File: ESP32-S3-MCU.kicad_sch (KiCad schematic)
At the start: 40 parts, among them SW1 RESET, SW2 BOOT, X1 32.768KHz

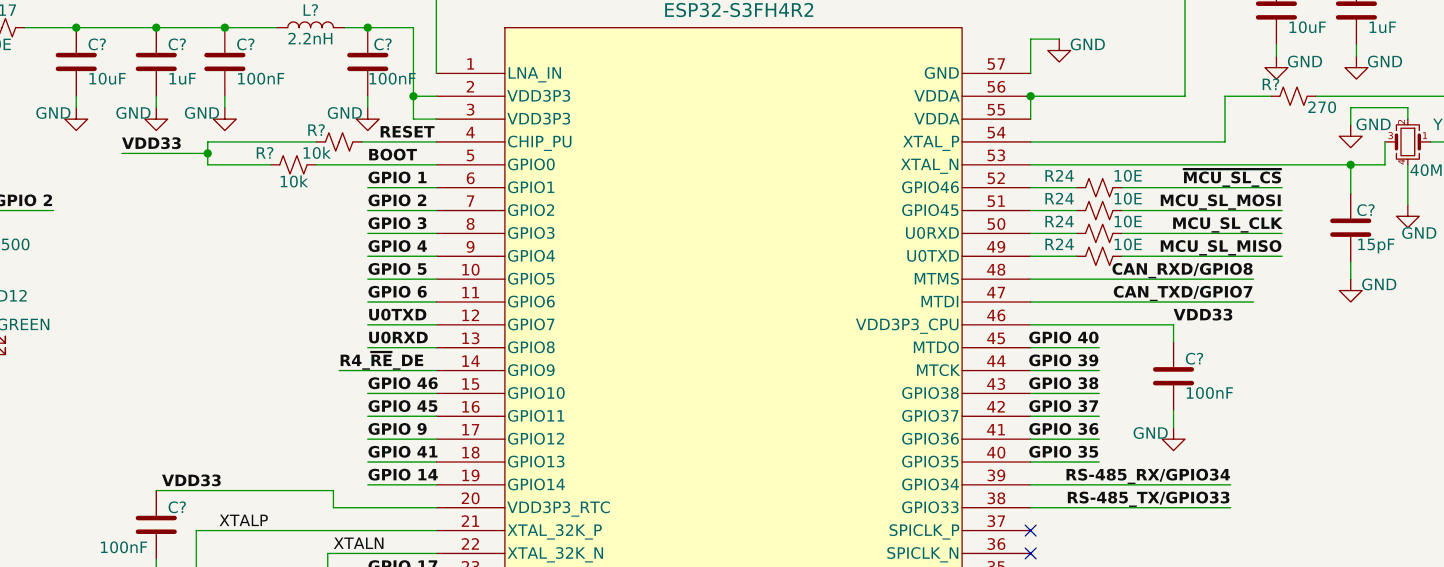
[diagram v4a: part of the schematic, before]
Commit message: Changed UART0 port connections
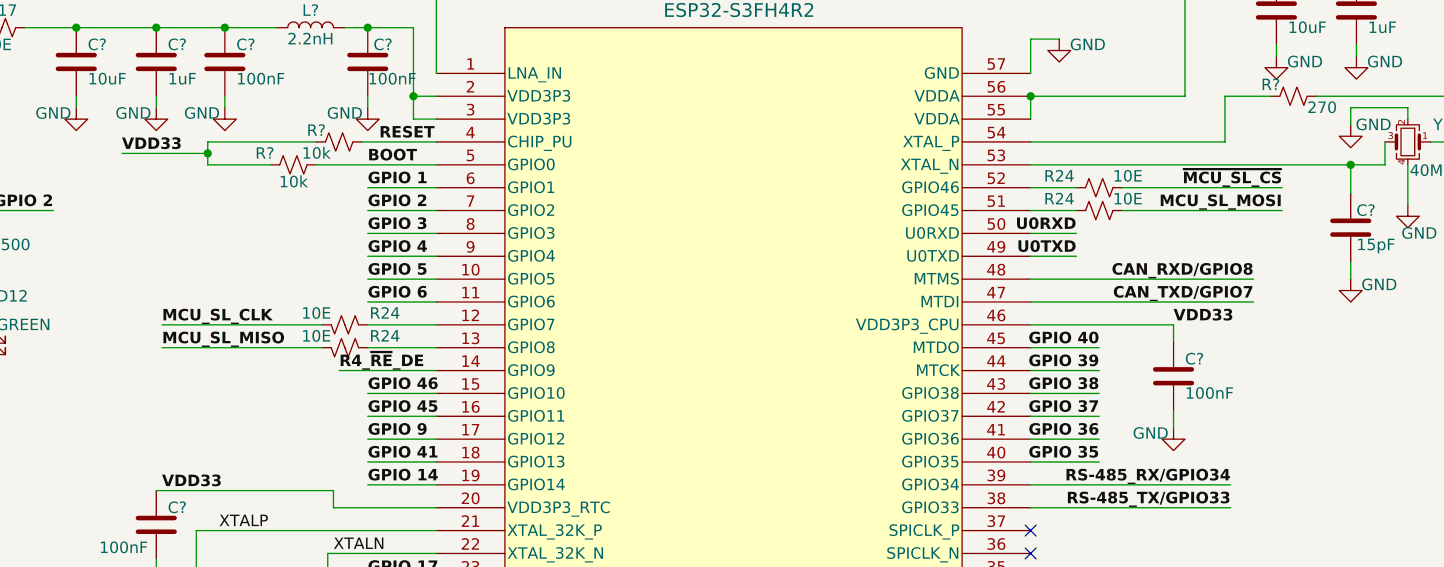
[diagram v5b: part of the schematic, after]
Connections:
- net BOOT_RXD: now also U?.50 (U0RXD); no longer U?.13 (GPIO8)
- net BOOT_TXD: now also U?.49 (U0TXD); no longer U?.12 (GPIO7)
- net at R24.1: now also U?.12 (GPIO7); no longer U?.50 (U0RXD)
- net at R24.2: now also U?.13 (GPIO8); no longer U?.49 (U0TXD)
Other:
- moved on the sheet: R24
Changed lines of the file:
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@@
     (stroke (width 0) (type default))
   )
-  (wire (pts (xy 215.265 80.01) (xy 197.485 80.01))
+  (wire (pts (xy 90.805 90.17) (xy 108.585 90.17))
     (stroke (width 0) (type default))
   )
@@
     (stroke (width 0) (type default))
   )
-  (wire (pts (xy 215.265 82.55) (xy 197.485 82.55))
+  (wire (pts (xy 90.805 92.71) (xy 108.585 92.71))
     (stroke (width 0) (type default))
   )
@@
     (effects (font (size 1.27 1.27) (thickness 0.254) bold (color 204 102 0 1)) (justify right bottom))
   )
-  (label "U0RXD" (at 113.665 92.71 0) (fields_autoplaced)
-    (effects (font (size 1.27 1.27) bold (color 0 0 255 1)) (justify left bottom))
-  )
-  (label "MCU_SL_MISO" (at 215.265 82.55 180) (fields_autoplaced)
-    (effects (font (size 1.27 1.27) (thickness 0.254) bold (color 204 102 0 1)) (justify right bottom))
-  )
-  (label "MCU_SL_CLK" (at 215.265 80.01 180) (fields_autoplaced)
-    (effects (font (size 1.27 1.27) (thickness 0.254) bold (color 204 102 0 1)) (justify right bottom))
+  (label "U0RXD" (at 192.405 80.01 180) (fields_autoplaced)
+    (effects (font (size 1.27 1.27) bold (color 0 0 255 1)) (justify right bottom))
+  )
+  (label "MCU_SL_MISO" (at 90.805 92.71 0) (fields_autoplaced)
+    (effects (font (size 1.27 1.27) (thickness 0.254) bold (color 204 102 0 1)) (justify left bottom))
+  )
+  (label "MCU_SL_CLK" (at 90.805 90.17 0) (fields_autoplaced)
+    (effects (font (size 1.27 1.27) (thickness 0.254) bold (color 204 102 0 1)) (justify left bottom))
   )
   (label "GPIO 40" (at 118.745 163.322 180) (fields_autoplaced)
@@
     (effects (font (size 1.27 1.27) bold (color 0 132 0 1)) (justify left bottom))
   )
-  (label "U0TXD" (at 113.665 90.17 0) (fields_autoplaced)
-    (effects (font (size 1.27 1.27) bold (color 0 0 255 1)) (justify left bottom))
+  (label "U0TXD" (at 192.405 82.55 180) (fields_autoplaced)
+    (effects (font (size 1.27 1.27) bold (color 0 0 255 1)) (justify right bottom))
   )
   (label "GPIO 3" (at 92.075 155.702 180) (fields_autoplaced)
@@
     )
   )
-  (symbol (lib_id "ESP32-S3_DB:R_Small_US") (at 194.945 80.01 90) (unit 1)
-    (in_bom yes) (on_board yes) (dnp no)
-    (property "Reference" "R24" (at 190.5 78.74 90)
-      (effects (font (size 1.27 1.27)))
-    )
-    (property "Value" "10E" (at 198.12 78.74 90)
-      (effects (font (size 1.27 1.27)))
-    )
-    (property "Footprint" "ESP32-S3_Dev_Board:R_0402_1005Metric" (at 194.945 80.01 0)
-      (effects (font (size 1.27 1.27)) hide)
-    )
-    (property "Datasheet" "~" (at 194.945 80.01 0)
-      (effects (font (size 1.27 1.27)) hide)
-    )
-    (property "PN" "RTT02100JTH" (at 194.945 80.01 0)
+  (symbol (lib_id "ESP32-S3_DB:R_Small_US") (at 111.125 90.17 270) (mirror x) (unit 1)
+    (in_bom yes) (on_board yes) (dnp no)
+    (property "Reference" "R24" (at 115.57 88.9 90)
+      (effects (font (size 1.27 1.27)))
+    )
+    (property "Value" "10E" (at 107.95 88.9 90)
+      (effects (font (size 1.27 1.27)))
+    )
+    (property "Footprint" "ESP32-S3_Dev_Board:R_0402_1005Metric" (at 111.125 90.17 0)
+      (effects (font (size 1.27 1.27)) hide)
+    )
+    (property "Datasheet" "~" (at 111.125 90.17 0)
+      (effects (font (size 1.27 1.27)) hide)
+    )
+    (property "PN" "RTT02100JTH" (at 111.125 90.17 0)
       (effects (font (size 1.27 1.27)) hide)
     )
@@
     )
   )
-  (symbol (lib_id "ESP32-S3_DB:R_Small_US") (at 194.945 82.55 270) (unit 1)
-    (in_bom yes) (on_board yes) (dnp no)
-    (property "Reference" "R24" (at 190.5 81.28 90)
-      (effects (font (size 1.27 1.27)))
-    )
-    (property "Value" "10E" (at 198.12 81.28 90)
-      (effects (font (size 1.27 1.27)))
-    )
-    (property "Footprint" "ESP32-S3_Dev_Board:R_0402_1005Metric" (at 194.945 82.55 0)
-      (effects (font (size 1.27 1.27)) hide)
-    )
-    (property "Datasheet" "~" (at 194.945 82.55 0)
-      (effects (font (size 1.27 1.27)) hide)
-    )
-    (property "PN" "RTT02100JTH" (at 194.945 82.55 0)
-      (effects (font (size 1.27 1.27)) hide)
-    )
+  (symbol (lib_id "ESP32-S3_DB:R_Small_US") (at 111.125 92.71 90) (mirror x) (unit 1)
+    (in_bom yes) (on_board yes) (dnp no)
+    (property "Reference" "R24" (at 115.57 91.44 90)
+      (effects (font (size 1.27 1.27)))
+    )
+    (property "Value" "10E" (at 107.95 91.44 90)
+      (effects (font (size 1.27 1.27)))
+    )
+    (property "Footprint" "ESP32-S3_Dev_Board:R_0402_1005Metric" (at 111.125 92.71 0)
+      (effects (font (size 1.27 1.27)) hide)
+    )
+    (property "Datasheet" "~" (at 111.125 92.71 0)
+      (effects (font (size 1.27 1.27)) hide)
+    )
+    (property "PN" "RTT02100JTH" (at 111.125 92.71 0)
+      (effects (font (size 1.27 1.27)) hide)
+    )

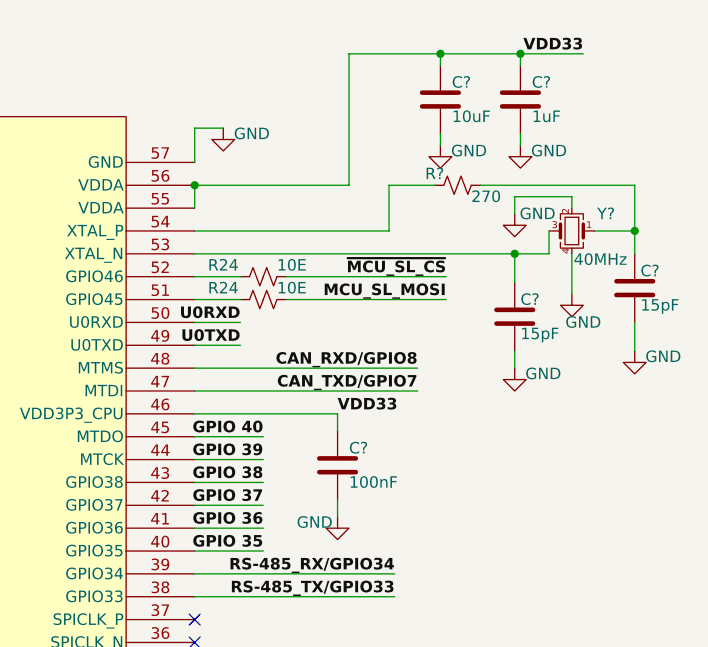
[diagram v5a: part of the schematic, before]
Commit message: Changed GPIO39, 40 crossing and added GND vias near other vias
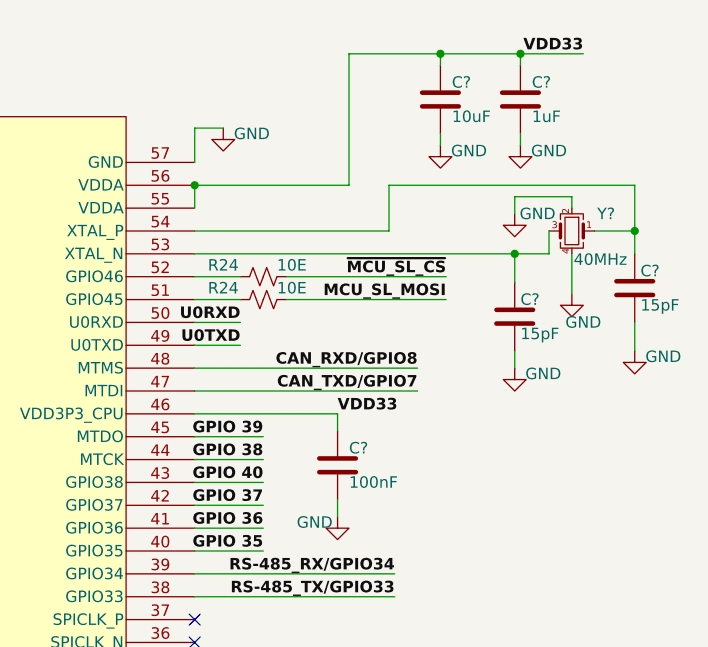
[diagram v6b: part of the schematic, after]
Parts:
- removed R?: 270, ESP32-S3_Dev_Board:R_0402_1005Metric, symbol ESP32-S3_DB:R_Small_US
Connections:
- net GPIO38: now also U?.44 (MTCK); no longer U?.43 (GPIO38)
- net GPIO39: now also U?.45 (MTDO); no longer U?.44 (MTCK)
- net GPIO40: now also U?.43 (GPIO38); no longer U?.45 (MTDO)
- net at C?.1, Y?.1: now also U?.54 (XTAL_P)
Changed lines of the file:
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@@
     (stroke (width 0) (type default))
   )
-  (wire (pts (xy 219.075 64.77) (xy 236.22 64.77))
+  (wire (pts (xy 208.915 64.77) (xy 236.22 64.77))
     (stroke (width 0) (type default))
   )
@@
   )
   (wire (pts (xy 97.79 57.15) (xy 103.505 57.15))
-    (stroke (width 0) (type default))
-  )
-  (wire (pts (xy 208.915 64.77) (xy 213.995 64.77))
     (stroke (width 0) (type default))
   )
@@
     (effects (font (size 1.27 1.27) (thickness 0.254) bold (color 204 102 0 1)) (justify left bottom))
   )
-  (label "GPIO 39" (at 194.945 95.25 180) (fields_autoplaced)
+  (label "GPIO 39" (at 194.945 92.71 180) (fields_autoplaced)
     (effects (font (size 1.27 1.27) bold (color 0 132 0 1)) (justify right bottom))
   )
@@
     (effects (font (size 1.27 1.27) bold (color 0 132 0 1)) (justify left bottom))
   )
-  (label "GPIO 38" (at 194.945 97.79 180) (fields_autoplaced)
+  (label "GPIO 38" (at 194.945 95.25 180) (fields_autoplaced)
     (effects (font (size 1.27 1.27) bold (color 0 132 0 1)) (justify right bottom))
   )
@@
     (effects (font (size 1.27 1.27) bold (color 0 132 0 1)) (justify left bottom))
   )
-  (label "GPIO 40" (at 194.945 92.71 180) (fields_autoplaced)
+  (label "GPIO 40" (at 194.945 97.79 180) (fields_autoplaced)
     (effects (font (size 1.27 1.27) bold (color 0 132 0 1)) (justify right bottom))
   )
@@
         )
       )
-    )
-  )
-  (symbol (lib_id "ESP32-S3_DB:R_Small_US") (at 216.535 64.77 90) (unit 1)
-    (in_bom yes) (on_board yes) (dnp no)
-    (property "Reference" "R?" (at 213.995 63.5 90)
-      (effects (font (size 1.27 1.27)))
-    )
-    (property "Value" "270" (at 219.71 66.04 90)
-      (effects (font (size 1.27 1.27)))
-    )
-    (property "Footprint" "ESP32-S3_Dev_Board:R_0402_1005Metric" (at 216.535 64.77 0)
-      (effects (font (size 1.27 1.27)) hide)
-    )
-    (property "Datasheet" "~" (at 216.535 64.77 0)
-      (effects (font (size 1.27 1.27)) hide)
-    )
-    (property "PN" "RC0402FR-07270RL" (at 216.535 64.77 0)
-      (effects (font (size 1.27 1.27)) hide)
-    )
-    (pin "1")
-    (pin "2")
-    (instances
-      (project "ESP32-S3_DB"
-        (path "/b7fc4bd3-c219-4455-832b-8d795385dcf1"
-          (reference "R?") (unit 1)
-        )
-        (path "/b7fc4bd3-c219-4455-832b-8d795385dcf1/cd99bb00-fc75-4430-bf94-ba56f480f215"
-          (reference "R2") (unit 1)
-        )
-      )

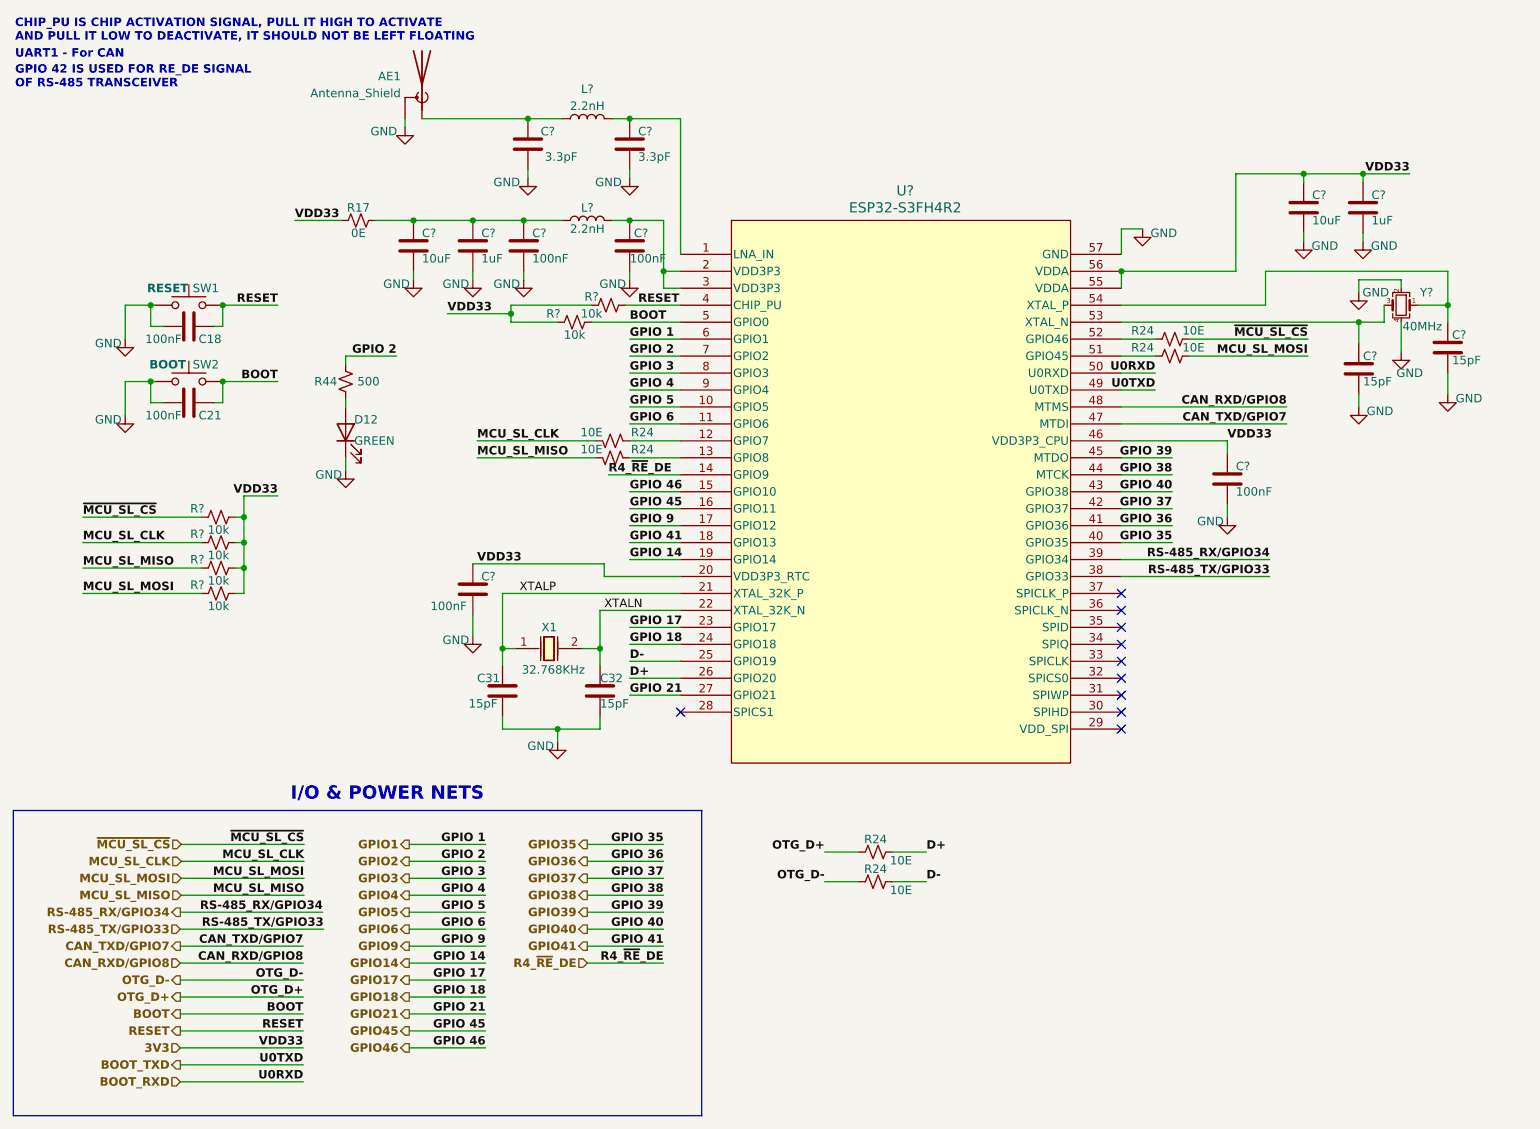
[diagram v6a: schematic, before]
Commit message: Changed pin mapping for ESP
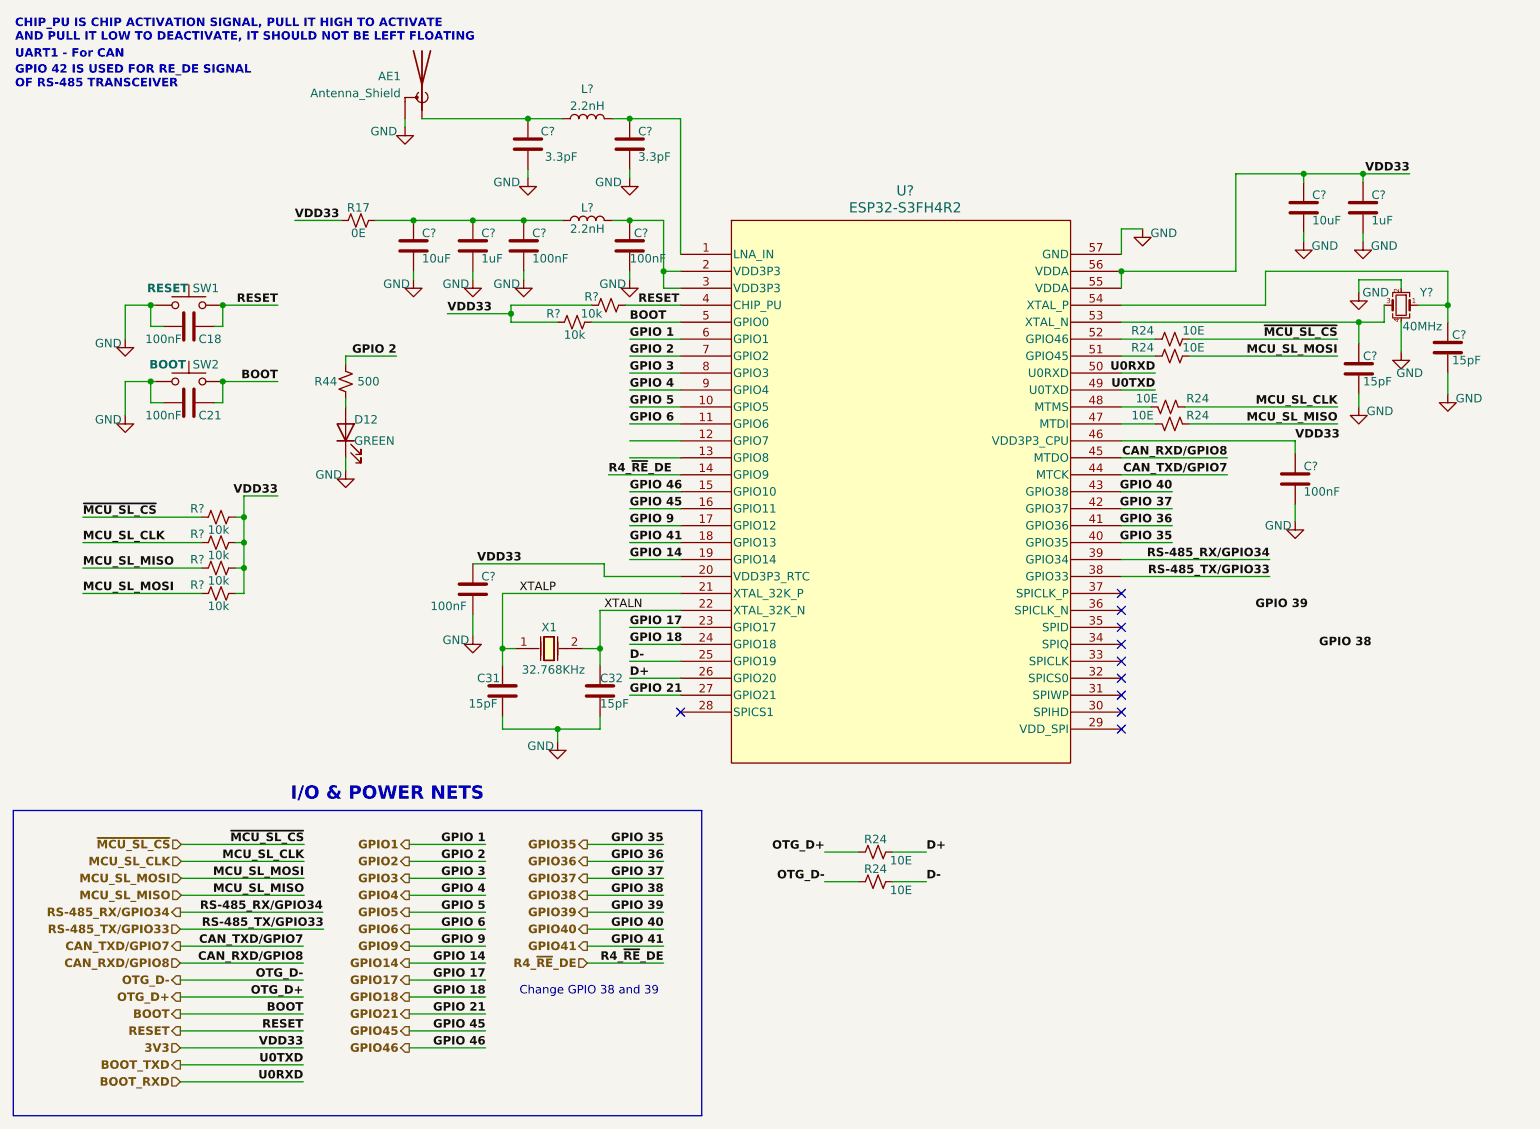
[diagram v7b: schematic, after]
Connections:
- net CAN_RXD/GPIO8: now also U?.45 (MTDO); no longer U?.48 (MTMS)
- net CAN_TXD/GPIO7: now also U?.44 (MTCK); no longer U?.47 (MTDI)
- net GPIO38: no longer U?.44 (MTCK)
- net GPIO39: no longer U?.45 (MTDO)
- net MCU_SL_CLK: now also R24.1; no longer R24.2
- net MCU_SL_MISO: now also R24.2; no longer R24.1
- net at U?.12 (GPIO7): no longer R24.1
- net at U?.13 (GPIO8): no longer R24.2
- new net: R24.2, U?.48 (MTMS)
- new net: R24.1, U?.47 (MTDI)
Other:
- note added: "Change GPIO 38 and 39"
- moved on the sheet: C?, R24
